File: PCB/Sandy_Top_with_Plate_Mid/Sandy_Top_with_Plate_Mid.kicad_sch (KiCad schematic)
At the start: 74 parts, among them J1 Conn_02x02_Top_Bottom, J2 Conn_02x02_Top_Bottom, J3 Conn_02x02_Top_Bottom

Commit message: ネジ穴調整、追加
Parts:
- removed D15: D, locallib:D_SOD-123_Emphasized_Direction_Line, symbol Device:D
- removed EXT_TC7: Conn_01x01, TestPoint:TestPoint_THTPad_D2.0mm_Drill1.0mm, symbol Connector_Generic:Conn_01x01
- removed SW_=1: SW_Push, MX_Alps_Hybrid:MXOnly-1U-Hotswap-guide, symbol Switch:SW_Push
- added H10, H11, H12, H9: MountingHole, locallib:MountingHole_2.2mm_M2_Pad_minimal, symbol Mechanical:MountingHole_Pad
- renumbered SW_6 to SW_-1, SW_\1 to SW_6, SW_`1 to SW_=1, SW_-1 to SW_INS1
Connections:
- net Top_GND: no longer H1.1, H2.1, H3.1, H4.1, H5.1, H6.1, H7.1, H8.1
- net Top_col7: no longer J1.4 (Pin_4)
- net col7: no longer names the net of #J3.4 (Pin_4), #J6.4a (Pin_4a)
- net col7: no longer #J13.4a (Pin_4a), #J9.4 (Pin_4)
- new net: #J13.4a (Pin_4a), #J9.4 (Pin_4)
- no-connect marks 0 -> 1
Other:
- note added: "Mid to Top: require 12 pins ( = 4 row + 7 col + GND )"
- note removed: "Mid to Top: require 12 pins"
- moved on the sheet: EXT_TR0, EXT_TR1, EXT_TR5, EXT_TR6, H2, H3, H4, H5, H6, H7, H8

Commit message: 基板間ピン割り当て
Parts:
- removed #J10: Conn_02x02_Row_Letter_Last, symbol Connector_Generic:Conn_02x02_Row_Letter_Last
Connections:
- net Top_col7 is gone; now on net Top_GND: #J13.4b (Pin_4b)
- net GND: now also #J13.4a (Pin_4a), #J9.4 (Pin_4)
- net Top_GND: now also H8.1, J1.4 (Pin_4)
- net Top_col0: now also H1.1
- net Top_col1: now also H6.1
- net Top_col2: now also H2.1
- net Top_col3: now also H7.1
- net Top_col4: now also H3.1
- net Top_col5: now also H9.1
- net Top_col6: now also H4.1
- net Top_row0: now also H5.1
- net Top_row1: now also H11.1
- net Top_row5: now also H10.1
- net Top_row6: now also H12.1
- no-connect marks 1 -> 0
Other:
- moved on the sheet: H1, H10, H11, H12, H2, H3, H4, H5

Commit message: ネジ穴と接続するピンを調整中
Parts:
- added D15, D20: D, locallib:D_SOD-123_Emphasized_Direction_Line, symbol Device:D
- added EXT_TR2: Conn_01x01, TestPoint:TestPoint_THTPad_D2.0mm_Drill1.0mm, symbol Connector_Generic:Conn_01x01
- added H13: MountingHole, locallib:MountingHole_2.2mm_M2_Pad_minimal, symbol Mechanical:MountingHole_Pad
- added SW_'1, SW_;1: SW_Push, MX_Alps_Hybrid:MXOnly-1U-Hotswap-guide, symbol Switch:SW_Push
- renumbered H5 to H11, H11 to H12, H6 to H5, H7 to H6, H8 to H7, H9 to H8, H12 to H9
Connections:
- net Top_GND: now also H10.1; no longer H7.1
- net Top_col2: now also H6.1; no longer H2.1
- net Top_col3: now also H2.1, SW_;1.1; no longer H6.1
- net Top_col4: now also SW_'1.2
- net Top_col5: now also H7.1; no longer H8.1
- net Top_row5: now also H8.1; no longer H10.1
- new net: D20.2 (A), SW_'1.1
- new net: D15.2 (A), SW_;1.2
- new net Top_row2: D15.1 (K), D20.1 (K), EXT_TR2.1 (Pin_1), H13.1
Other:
- moved on the sheet: D1, D10, D11, D12, D13, D14, D16, D17, D18, D19, D2, D3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

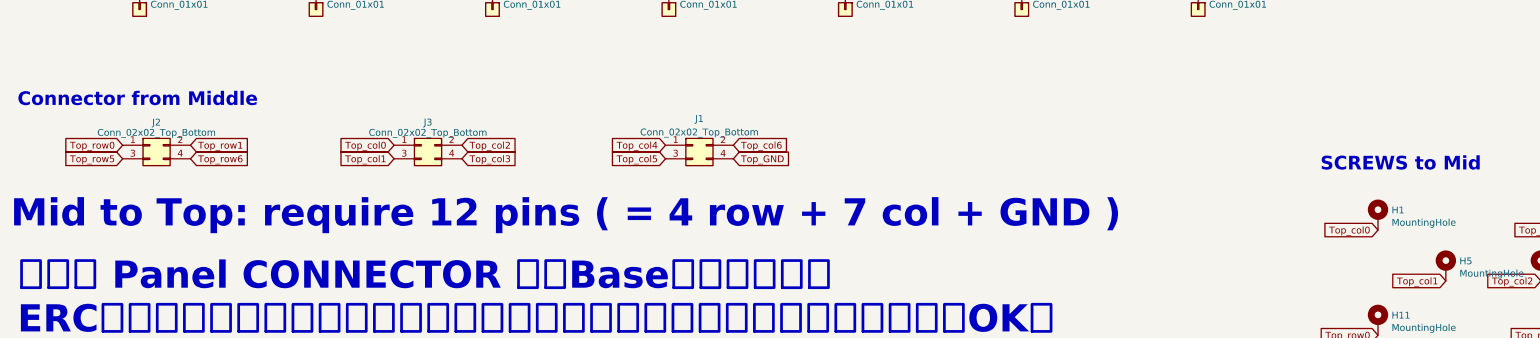
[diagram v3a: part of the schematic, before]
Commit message: ネジ穴と接続するピンを調整中
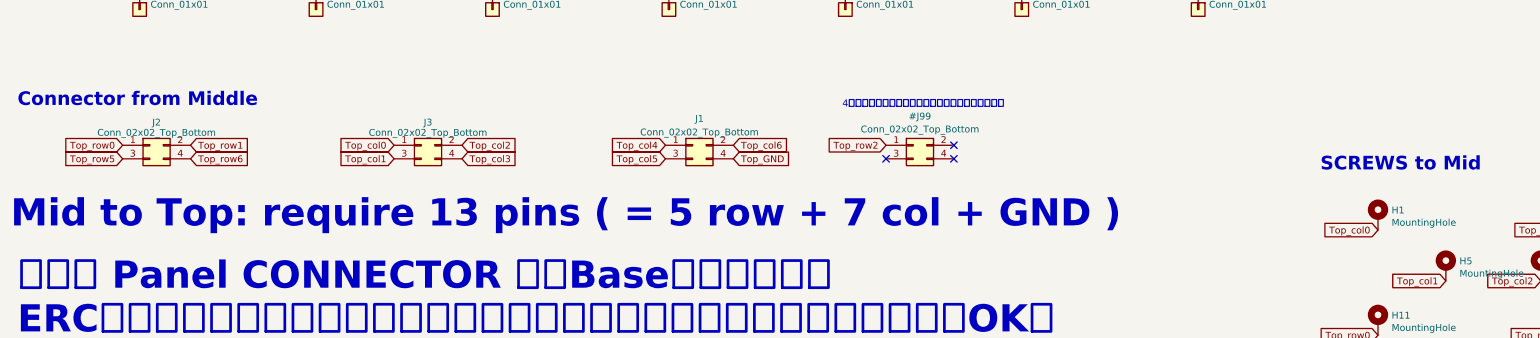
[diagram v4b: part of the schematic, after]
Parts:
- added #J99: Conn_02x02_Top_Bottom, locallib:JST_SH_SM04B-SRSS-TB_1x04-1MP_P1.00mm_Horizontal_wCable_housing_spare_pin, symbol Connector_Generic:Conn_02x02_Odd_Even
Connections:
- net Top_row2: now also #J99.1 (Pin_1)
- no-connect marks 0 -> 3
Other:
- note added: "4個目のコネクタは実際に配置していないのでダミー"
- note added: "Mid to Top: require 13 pins ( = 5 row + 7 col + GND )"
- note removed: "Mid to Top: require 12 pins ( = 4 row + 7 col + GND )"
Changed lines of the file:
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@@
 		(color 0 0 0 0)
 	)
+	(no_connect
+		(at 191.77 137.795)
+	)
+	(no_connect
+		(at 191.77 140.335)
+	)
+	(no_connect
+		(at 179.07 140.335)
+	)
 	(wire
 		(pts
@@
 		)
 	)
-	(text "Mid to Top: require 12 pins ( = 4 row + 7 col + GND )"
+	(text "4個目のコネクタは実際に配置していないのでダミー"
+		(exclude_from_sim no)
+		(at 186.055 130.175 0)
+		(effects
+			(font
+				(size 1.27 1.27)
+			)
+		)
+	)
+	(text "Mid to Top: require 13 pins ( = 5 row + 7 col + GND )"
 		(exclude_from_sim no)
 		(at 15.24 153.67 0)
@@
 		)
 	)
+	(global_label "Top_row2"
+		(shape input)
+		(at 179.07 137.795 180)
+		(fields_autoplaced yes)
+		(effects
+			(font
+				(size 1.27 1.27)
+			)
+			(justify right)
+		)
+		(property "Intersheetrefs" "${INTERSHEET_REFS}"
+			(at 168.0306 137.795 0)
+			(effects
+				(font
+					(size 1.27 1.27)
+				)
+				(justify right)
+				(hide yes)
+			)
+		)
+		(property "シート間のリファレンス" "${INTERSHEET_REFS}"
+			(at 179.07 139.6302 0)
+			(effects
+				(font
+					(size 1.27 1.27)
+				)
+				(justify right)
+				(hide yes)
+			)
+		)
+	)
 	(global_label "Mid_col6"
 		(shape input)
@@
 					(unit 1)
 				)
+			)
+		)
+	)
+	(symbol
+		(lib_id "Connector_Generic:Conn_02x02_Odd_Even")
+		(at 184.15 137.795 0)
+		(unit 1)
+		(exclude_from_sim no)
+		(in_bom yes)
+		(on_board yes)
+		(dnp no)
+		(fields_autoplaced yes)
+		(property "Reference" "#J99"
+			(at 185.42 132.3805 0)
+			(effects
+				(font
+					(size 1.27 1.27)
+				)
+			)
+		)
+		(property "Value" "Conn_02x02_Top_Bottom"
+			(at 185.42 134.8048 0)
+			(effects
+				(font
+					(size 1.27 1.27)
+				)
+			)
+		)
+		(property "Footprint" "locallib:JST_SH_SM04B-SRSS-TB_1x04-1MP_P1.00mm_Horizontal_wCable_housing_spare_pin"
+			(at 184.15 137.795 0)
+			(effects
+				(font
+					(size 1.27 1.27)
+				)
+				(hide yes)
+			)
+		)
+		(property "Datasheet" "~"
+			(at 184.15 137.795 0)
+			(effects
+				(font
+					(size 1.27 1.27)
+				)
+				(hide yes)
+			)
+		)
+		(property "Description" ""
+			(at 184.15 137.795 0)
+			(effects
+				(font
+					(size 1.27 1.27)
+				)
+				(hide yes)
+			)
+		)
+		(property "LCSC" "C371510"
+			(at 184.15 137.795 0)
+			(effects
+				(font
+					(size 1.27 1.27)
+				)
+				(hide yes)
+			)
+		)
+		(pin "1"
+		)
+		(pin "2"
+		)
+		(pin "3"
+		)
+		(pin "4"
+		)
+		(instances
+			(project "Sandy_Top_with_Plate_Mid"
+				(path "/a99ab643-cdc7-4f8c-8088-c1f4faa914d1"
+					(reference "#J99")
+					(unit 1)
+				)

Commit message: ネジ位置調整
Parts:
- SW_-1: footprint MX_Alps_Hybrid:MXOnly-1U-Hotswap-screw-hole-side1-guide -> MX_Alps_Hybrid:MXOnly-1U-Hotswap-screw-hole-side3-guide
- SW_10, SW_2: footprint MX_Alps_Hybrid:MXOnly-1U-Hotswap-guide -> MX_Alps_Hybrid:MXOnly-1U-Hotswap-screw-hole-side3-guide
- SW_4, SW_INS1: footprint MX_Alps_Hybrid:MXOnly-1U-Hotswap-guide -> MX_Alps_Hybrid:MXOnly-1U-Hotswap-screw-hole-side1-guide
- SW_5: footprint MX_Alps_Hybrid:MXOnly-1U-Hotswap-screw-hole-side2-guide -> MX_Alps_Hybrid:MXOnly-1U-Hotswap-guide
- SW_6: footprint MX_Alps_Hybrid:MXOnly-1U-Hotswap-guide -> MX_Alps_Hybrid:MXOnly-1U-Hotswap-screw-hole-side2-guide
- SW_8: footprint MX_Alps_Hybrid:MXOnly-1U-Hotswap-screw-hole-side3-guide -> MX_Alps_Hybrid:MXOnly-1U-Hotswap-guide
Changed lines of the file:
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@@
 			)
 		)
-		(property "Footprint" "MX_Alps_Hybrid:MXOnly-1U-Hotswap-guide"
+		(property "Footprint" "MX_Alps_Hybrid:MXOnly-1U-Hotswap-screw-hole-side3-guide"
 			(at 77.47 39.37 0)
 			(effects
@@
 			)
 		)
-		(property "Footprint" "MX_Alps_Hybrid:MXOnly-1U-Hotswap-screw-hole-side1-guide"
+		(property "Footprint" "MX_Alps_Hybrid:MXOnly-1U-Hotswap-screw-hole-side3-guide"
 			(at 143.51 39.37 0)
 			(effects
@@
 			)
 		)
-		(property "Footprint" "MX_Alps_Hybrid:MXOnly-1U-Hotswap-guide"
+		(property "Footprint" "MX_Alps_Hybrid:MXOnly-1U-Hotswap-screw-hole-side1-guide"
 			(at 259.08 39.37 0)
 			(effects
@@
 			)
 		)
-		(property "Footprint" "MX_Alps_Hybrid:MXOnly-1U-Hotswap-screw-hole-side3-guide"
+		(property "Footprint" "MX_Alps_Hybrid:MXOnly-1U-Hotswap-guide"
 			(at 209.55 39.37 0)
 			(effects
@@
 			)
 		)
-		(property "Footprint" "MX_Alps_Hybrid:MXOnly-1U-Hotswap-screw-hole-side2-guide"
+		(property "Footprint" "MX_Alps_Hybrid:MXOnly-1U-Hotswap-guide"
 			(at 127 39.37 0)
 			(effects
@@
 			)
 		)
-		(property "Footprint" "MX_Alps_Hybrid:MXOnly-1U-Hotswap-guide"
+		(property "Footprint" "MX_Alps_Hybrid:MXOnly-1U-Hotswap-screw-hole-side3-guide"
 			(at 242.57 39.37 0)
 			(effects
@@
 			)
 		)
-		(property "Footprint" "MX_Alps_Hybrid:MXOnly-1U-Hotswap-guide"
+		(property "Footprint" "MX_Alps_Hybrid:MXOnly-1U-Hotswap-screw-hole-side1-guide"
 			(at 110.49 39.37 0)
 			(effects
@@
 			)
 		)
-		(property "Footprint" "MX_Alps_Hybrid:MXOnly-1U-Hotswap-guide"
+		(property "Footprint" "MX_Alps_Hybrid:MXOnly-1U-Hotswap-screw-hole-side2-guide"
 			(at 176.53 39.37 0)
 			(effects

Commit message: JST SH コネクタのフットプリントにコートヤードを追加
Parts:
- J1, J2, J3: footprint locallib:JST_SH_SM04B-SRSS-TB_1x04-1MP_P1.00mm_Horizontal_wCable_housing_spare_pin -> locallib:JST_SH_SM04B-SRSS-TB_1x04-1MP_P1.00mm_Horizontal_wCable_housing_spare_pin_courtyard
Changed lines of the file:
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@@
 			)
 		)
-		(property "Footprint" "locallib:JST_SH_SM04B-SRSS-TB_1x04-1MP_P1.00mm_Horizontal_wCable_housing_spare_pin"
+		(property "Footprint" "locallib:JST_SH_SM04B-SRSS-TB_1x04-1MP_P1.00mm_Horizontal_wCable_housing_spare_pin_courtyard"
 			(at 92.075 137.795 0)
 			(effects
@@
 			)
 		)
-		(property "Footprint" "locallib:JST_SH_SM04B-SRSS-TB_1x04-1MP_P1.00mm_Horizontal_wCable_housing_spare_pin"
+		(property "Footprint" "locallib:JST_SH_SM04B-SRSS-TB_1x04-1MP_P1.00mm_Horizontal_wCable_housing_spare_pin_courtyard"
 			(at 41.275 137.795 0)
 			(effects
@@
 			)
 		)
-		(property "Footprint" "locallib:JST_SH_SM04B-SRSS-TB_1x04-1MP_P1.00mm_Horizontal_wCable_housing_spare_pin"
+		(property "Footprint" "locallib:JST_SH_SM04B-SRSS-TB_1x04-1MP_P1.00mm_Horizontal_wCable_housing_spare_pin_courtyard"
 			(at 142.875 137.795 0)
 			(effects

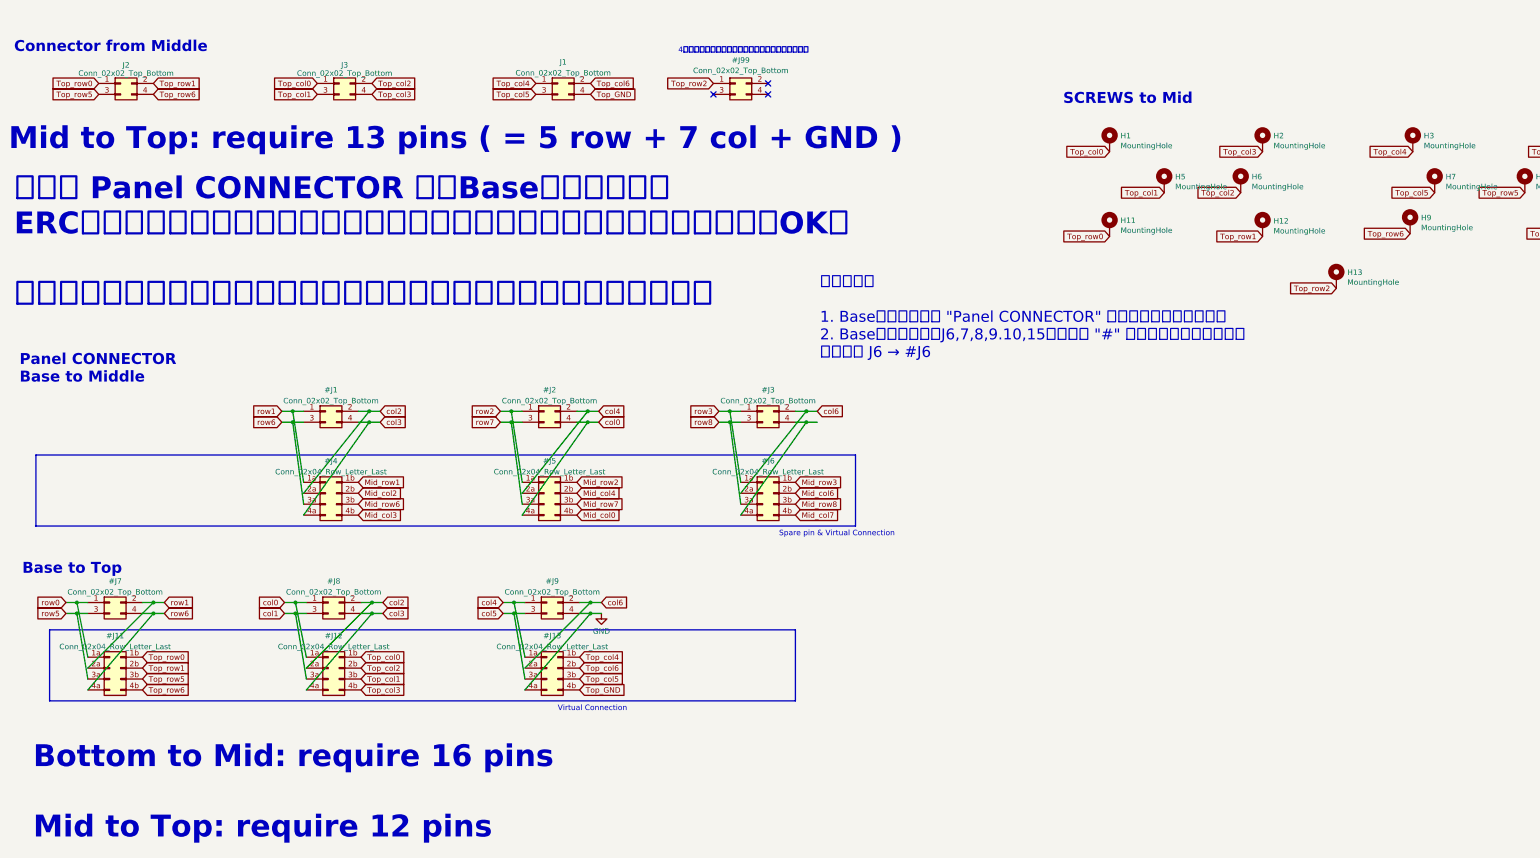
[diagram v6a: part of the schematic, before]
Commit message: SHコネクタで接続するピンを指定
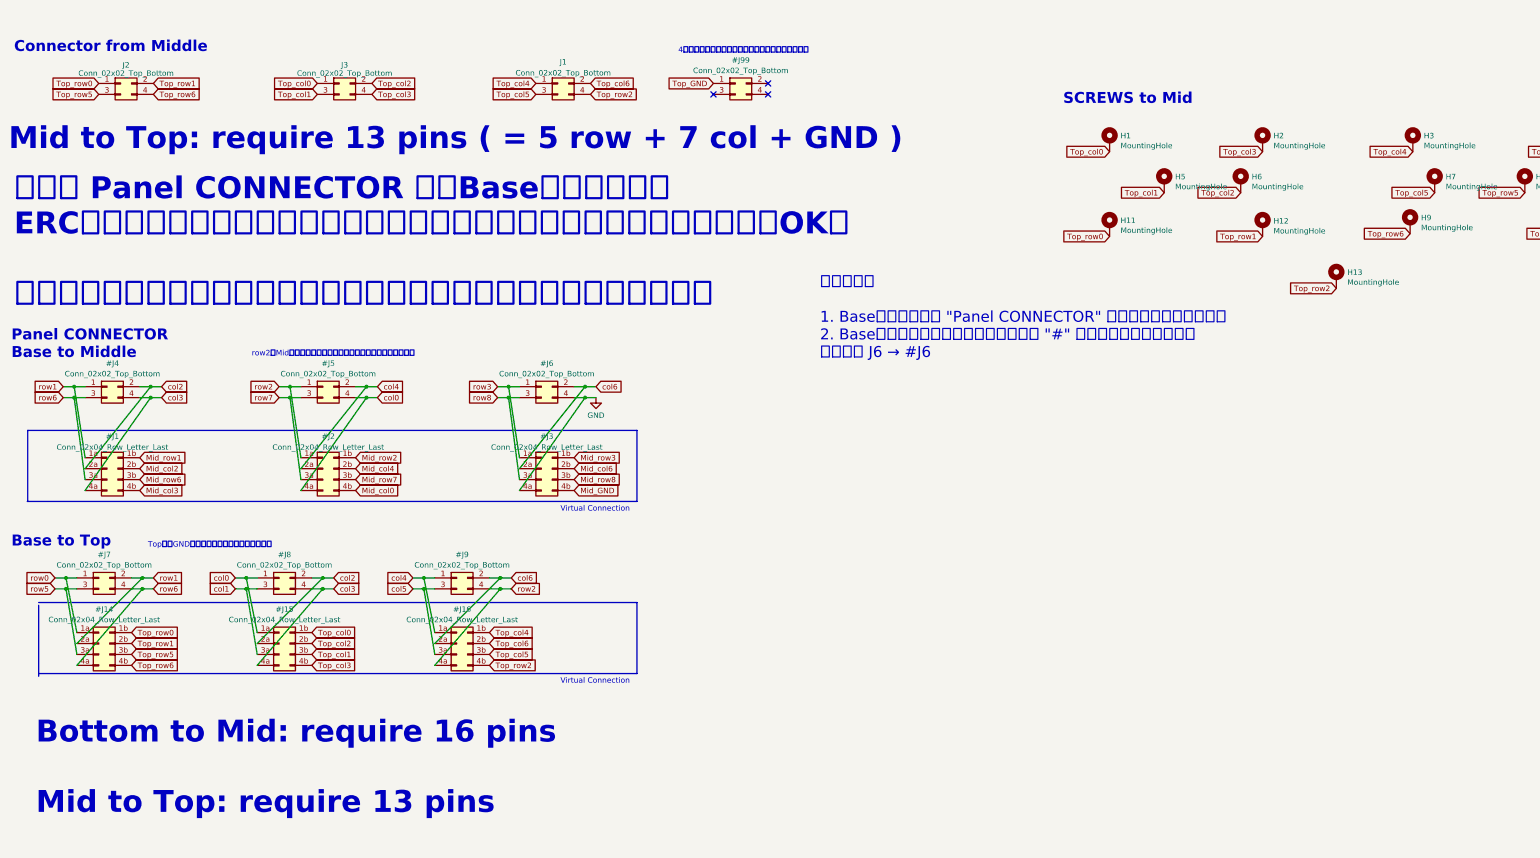
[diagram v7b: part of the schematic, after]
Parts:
- removed #J1, #J2, #J3: Conn_02x02_Top_Bottom, locallib:JST_SH_SM04B-SRSS-TB_1x04-1MP_P1.00mm_Horizontal_wCable_housing_spare_pin, symbol Connector_Generic:Conn_02x02_Odd_Even
- removed #J11, #J12, #J13, #J4, #J5, #J6: Conn_02x04_Row_Letter_Last, symbol Connector_Generic:Conn_02x04_Row_Letter_Last
- added #J1, #J14, #J15, #J16, #J2, #J3: Conn_02x04_Row_Letter_Last, symbol Connector_Generic:Conn_02x04_Row_Letter_Last
- added #J4, #J5, #J6: Conn_02x02_Top_Bottom, locallib:JST_SH_SM04B-SRSS-TB_1x04-1MP_P1.00mm_Horizontal_wCable_housing_spare_pin_courtyard, symbol Connector_Generic:Conn_02x02_Odd_Even
- #J7, #J8, #J9: footprint locallib:JST_SH_SM04B-SRSS-TB_1x04-1MP_P1.00mm_Horizontal_wCable_housing_spare_pin -> locallib:JST_SH_SM04B-SRSS-TB_1x04-1MP_P1.00mm_Horizontal_wCable_housing_spare_pin_courtyard; LCSC (none) -> C371510
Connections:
- net GND: now also #J3.4a (Pin_4a), #J6.4 (Pin_4); no longer #J9.4 (Pin_4)
- net Mid_col0: now also #J2.4b (Pin_4b)
- net Mid_col2: now also #J1.2b (Pin_2b)
- net Mid_col3: now also #J1.4b (Pin_4b)
- net Mid_col4: now also #J2.2b (Pin_2b)
- net Mid_col6: now also #J3.2b (Pin_2b)
- net Mid_row1: now also #J1.1b (Pin_1b)
- net Mid_row2: now also #J2.1b (Pin_1b)
- net Mid_row3: now also #J3.1b (Pin_1b)
- net Mid_row6: now also #J1.3b (Pin_3b)
- net Mid_row7: now also #J2.3b (Pin_3b)
- net Mid_row8: now also #J3.3b (Pin_3b)
- net Top_GND: now also #J99.1 (Pin_1); no longer J1.4 (Pin_4)
- net Top_col0: now also #J15.1b (Pin_1b)
- net Top_col1: now also #J15.3b (Pin_3b)
- net Top_col2: now also #J15.2b (Pin_2b)
- net Top_col3: now also #J15.4b (Pin_4b)
- net Top_col4: now also #J16.1b (Pin_1b)
- net Top_col5: now also #J16.3b (Pin_3b)
- net Top_col6: now also #J16.2b (Pin_2b)
- net Top_row0: now also #J14.1b (Pin_1b)
- net Top_row1: now also #J14.2b (Pin_2b)
- net Top_row2: now also J1.4 (Pin_4), #J16.4b (Pin_4b); no longer #J99.1 (Pin_1)
- net Top_row5: now also #J14.3b (Pin_3b)
- net Top_row6: now also #J14.4b (Pin_4b)
- net col0: now also #J15.1a (Pin_1a), #J2.4a (Pin_4a), #J5.4 (Pin_4)
- net col1: now also #J15.3a (Pin_3a)
- net col2: now also #J1.2a (Pin_2a), #J15.2a (Pin_2a), #J4.2 (Pin_2)
- net col3: now also #J1.4a (Pin_4a), #J15.4a (Pin_4a), #J4.4 (Pin_4)
- net col4: now also #J16.1a (Pin_1a), #J2.2a (Pin_2a), #J5.2 (Pin_2)
- net col5: now also #J16.3a (Pin_3a)
- net col6: now also #J16.2a (Pin_2a), #J3.2a (Pin_2a), #J6.2 (Pin_2)
- net row0: now also #J14.1a (Pin_1a)
- net row1: now also #J1.1a (Pin_1a), #J14.2a (Pin_2a), #J4.1 (Pin_1)
- net row2: now also #J9.4 (Pin_4), #J16.4a (Pin_4a), #J2.1a (Pin_1a), #J5.1 (Pin_1)
- net row3: now also #J3.1a (Pin_1a), #J6.1 (Pin_1)
- net row5: now also #J14.3a (Pin_3a)
- net row6: now also #J1.3a (Pin_3a), #J14.4a (Pin_4a), #J4.3 (Pin_3)
- net row7: now also #J2.3a (Pin_3a), #J5.3 (Pin_3)
- net row8: now also #J3.3a (Pin_3a), #J6.3 (Pin_3)
- new net Mid_GND: #J3.4b (Pin_4b)
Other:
- note added: "Bottom to Mid: require 16 pins Mid to Top: require 13 pins"
- note added: "TopへはGNDも送りたいが、ピンが足りない。"
- note added: "row2はMidで使用していないが、ピンが余っているので追加。"
- note added: "コピペ手順 1. Baseの回路図から "Panel CONNECTOR" の箇所をまるごとコピペ 2. Baseのコネクタのリファレンスの頭に "#" をつけて仮想シンボル化 例： J6 → #J6"
- note removed: "Bottom to Mid: require 16 pins Mid to Top: require 12 pins"
- note removed: "Spare pin & Virtual Connection"
- note removed: "コピペ手順 1. Baseの回路図から "Panel CONNECTOR" の箇所をまるごとコピペ 2. Baseのコネクタ（J6,7,8,9.10,15）の頭に "#" をつけて仮想シンボル化 例： J6 → #J6"
